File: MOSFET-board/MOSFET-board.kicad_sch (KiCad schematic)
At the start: 74 parts, among them J1 PCIE-LP-01-01-F-DV-A-TR, J2 DB25_Female, U1 BTS3080EJXUMA1, U10 BTS3080EJXUMA1, U11 PCF8575_Breakout, U2 BTS3080EJXUMA1, U3 BTS3080EJXUMA1, U4 BTS3080EJXUMA1, U5 BTS3080EJXUMA1, U6 BTS3080EJXUMA1, U7 BTS3080EJXUMA1, U8 BTS3080EJXUMA1, U9 BTS3080EJXUMA1

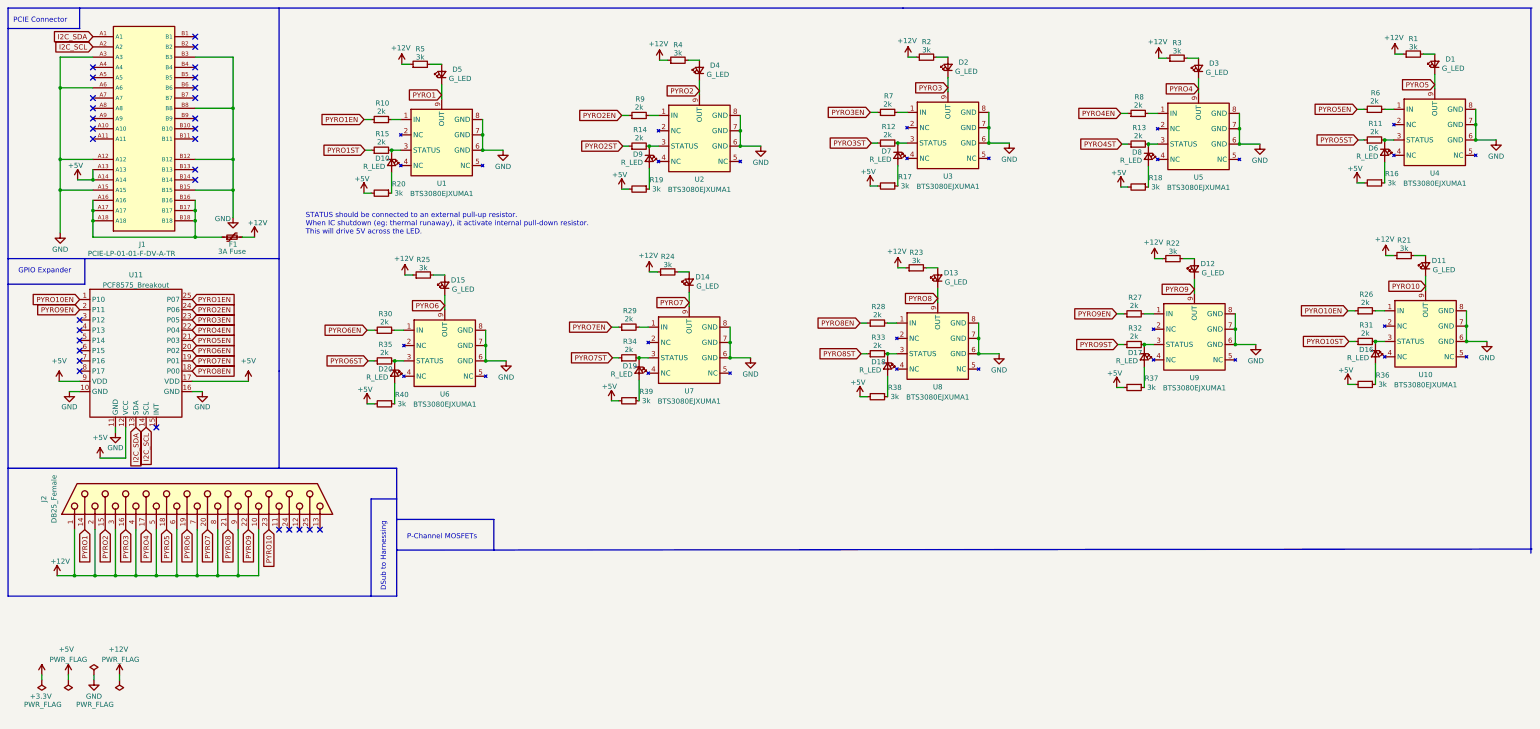
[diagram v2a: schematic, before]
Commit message: Updated HX, TC, and MOSFET board.
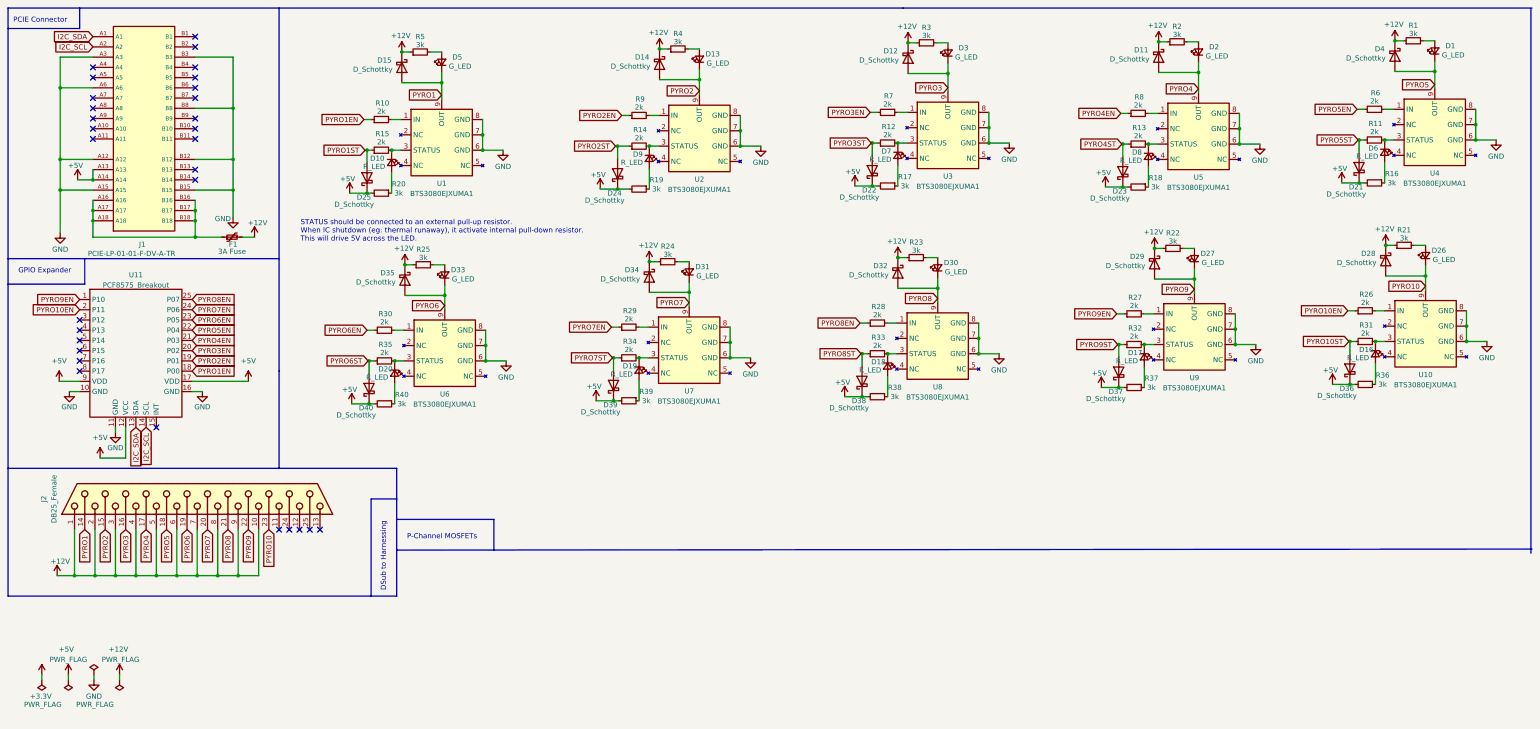
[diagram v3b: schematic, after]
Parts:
- removed D11, D12, D14, D15, D4: G_LED, LED_THT:LED_D1.8mm_W3.3mm_H2.4mm, symbol Device:LED_Small
- added D11, D12, D14, D15, D21, D22, D23, D24, D25, D28, D29, D32, D34, D35, D36, D37, D38, D39, D4, D40: D_Schottky, Diode_SMD:D_0603_1608Metric, symbol Device:D_Schottky
- added D26, D27, D30, D31, D33: G_LED, LED_THT:LED_D1.8mm_W3.3mm_H2.4mm, symbol Device:LED_Small
- F1: footprint (none) -> Fuse:Fuse_0603_1608Metric
- J1: footprint PCIe_x1_card_edge:PCIe_x1_card_edge -> Connector_PCBEdge:BUS_PCIexpress_x1
- R1, R10, R11, R12, R13, R14, R15, R16, R17, R18, R19, R2, R20, R21, R22, R23, R24, R25, R26, R27, R28, R29, R3, R30, R31, R32, R33, R34, R35, R36, R37, R38, R39, R4, R40, R5, R6, R7, R8, R9: footprint Resistor_SMD:R_0805_2012Metric -> Resistor_SMD:R_0603_1608Metric
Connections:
- net +12V: now also D11.1 (K), D12.1 (K), D14.1 (K), D15.1 (K), D28.1 (K), D29.1 (K), D32.1 (K), D34.1 (K), D35.1 (K), D4.1 (K)
- net +5V: now also D21.1 (K), D22.1 (K), D23.1 (K), D24.1 (K), D25.1 (K), D36.1 (K), D37.1 (K), D38.1 (K), D39.1 (K), D40.1 (K)
- net PYRO1: now also D15.2 (A)
- net PYRO10: now also D26.1 (K), D28.2 (A)
- net PYRO10EN: now also U11.2 (P11); no longer U11.1 (P10)
- net PYRO10ST: now also D36.2 (A)
- net PYRO1EN: now also U11.18 (P00); no longer U11.25 (P07)
- net PYRO1ST: now also D25.2 (A)
- net PYRO2: now also D13.1 (K), D14.2 (A)
- net PYRO2EN: now also U11.19 (P01); no longer U11.24 (P06)
- net PYRO2ST: now also D24.2 (A)
- net PYRO3: now also D3.1 (K), D12.2 (A); no longer D2.1 (K)
- net PYRO3EN: now also U11.20 (P02); no longer U11.23 (P05)
- net PYRO3ST: now also D22.2 (A)
- net PYRO4: now also D2.1 (K), D11.2 (A); no longer D3.1 (K)
- net PYRO4EN: now also U11.21 (P03); no longer U11.22 (P04)
- net PYRO4ST: now also D23.2 (A)
- net PYRO5: now also D4.2 (A)
- net PYRO5EN: now also U11.22 (P04); no longer U11.21 (P03)
- net PYRO5ST: now also D21.2 (A)
- net PYRO6: now also D33.1 (K), D35.2 (A)
- net PYRO6EN: now also U11.23 (P05); no longer U11.20 (P02)
- net PYRO6ST: now also D40.2 (A)
- net PYRO7: now also D31.1 (K), D34.2 (A)
- net PYRO7EN: now also U11.24 (P06); no longer U11.19 (P01)
- net PYRO7ST: now also D39.2 (A)
- net PYRO8: now also D30.1 (K), D32.2 (A); no longer D13.1 (K)
- net PYRO8EN: now also U11.25 (P07); no longer U11.18 (P00)
- net PYRO8ST: now also D38.2 (A)
- net PYRO9: now also D27.1 (K), D29.2 (A)
- net PYRO9EN: now also U11.1 (P10); no longer U11.2 (P11)
- net PYRO9ST: now also D37.2 (A)
- net at D13.2 (A): now also R4.2; no longer R23.2
- net at R25.2: now also D33.2 (A)
- net at R22.2: now also D27.2 (A)
- net at R24.2: now also D31.2 (A)
- net at R21.2: now also D26.2 (A)
- new net: D30.2 (A), R23.2
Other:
- moved on the sheet: D5, R5

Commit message: Updated pcie and fixed HX, MOSFET, TC board. Also added hierarchical sheet.
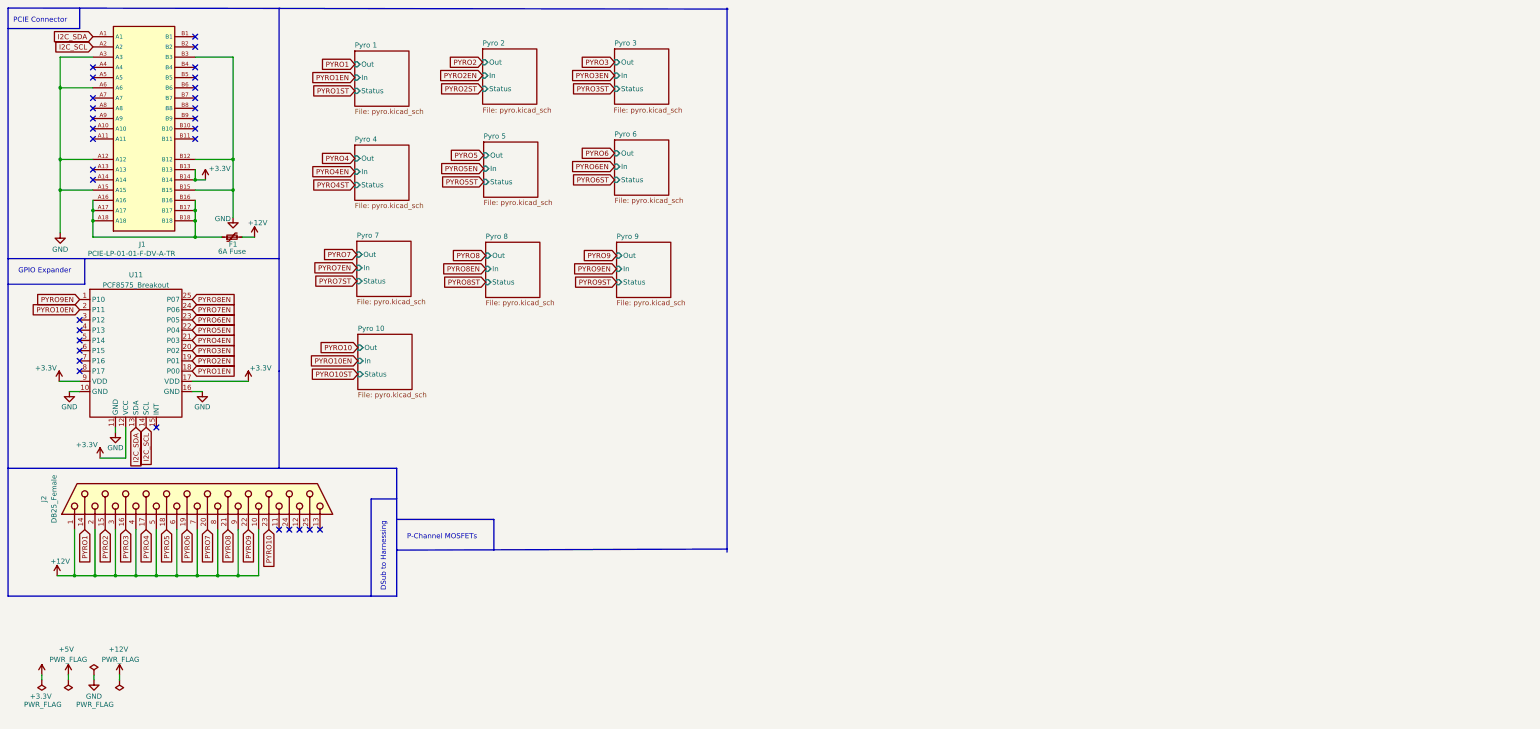
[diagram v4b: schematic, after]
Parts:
- removed D1, D13, D2, D26, D27, D3, D30, D31, D33, D5: G_LED, LED_THT:LED_D1.8mm_W3.3mm_H2.4mm, symbol Device:LED_Small
- removed D10, D16, D17, D18, D19, D20, D6, D7, D8, D9: R_LED, LED_THT:LED_D1.8mm_W3.3mm_H2.4mm, symbol Device:LED_Small
- removed D11, D12, D14, D15, D21, D22, D23, D24, D25, D28, D29, D32, D34, D35, D36, D37, D38, D39, D4, D40: D_Schottky, Diode_SMD:D_0603_1608Metric, symbol Device:D_Schottky
- removed R1, R16, R17, R18, R19, R2, R20, R21, R22, R23, R24, R25, R3, R36, R37, R38, R39, R4, R40, R5: 3k, Resistor_SMD:R_0603_1608Metric, symbol Device:R_Small
- removed R10, R11, R12, R13, R14, R15, R26, R27, R28, R29, R30, R31, R32, R33, R34, R35, R6, R7, R8, R9: 2k, Resistor_SMD:R_0603_1608Metric, symbol Device:R_Small
- removed U1, U10, U2, U3, U4, U5, U6, U7, U8, U9: BTS3080EJXUMA1, BTS3080EJXUMA1:SOIC127P600X115-9N, symbol BTS3080EJXUMA1:BTS3080EJXUMA1
- F1: value 3A Fuse -> 6A Fuse
- U11: footprint PCF875BreakoutBoard5:PCF8575_Breakout -> PCF8575_Breakout:PCF8575_Breakout
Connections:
- net +3.3V: now also J1.B13, J1.B14, U11.12 (VCC), U11.17 (VDD), U11.9 (VDD)
- net +5V: no longer J1.A13, J1.A14, U11.12 (VCC), U11.17 (VDD), U11.9 (VDD)
- net GND: no longer J1.B8
- no-connect marks 30 -> 31
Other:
- added sheet Pyro 1 (pyro.kicad_sch)
- added sheet Pyro 10 (pyro.kicad_sch)
- added sheet Pyro 2 (pyro.kicad_sch)
- added sheet Pyro 3 (pyro.kicad_sch)
- added sheet Pyro 4 (pyro.kicad_sch)
- added sheet Pyro 5 (pyro.kicad_sch)
- added sheet Pyro 6 (pyro.kicad_sch)
- added sheet Pyro 7 (pyro.kicad_sch)
- added sheet Pyro 8 (pyro.kicad_sch)
- added sheet Pyro 9 (pyro.kicad_sch)
- note removed: "STATUS should be connected to an external pull-up resistor. When IC shutdown (eg: thermal runaway), it activate internal pull-down resistor. This will drive 5V across the LED."

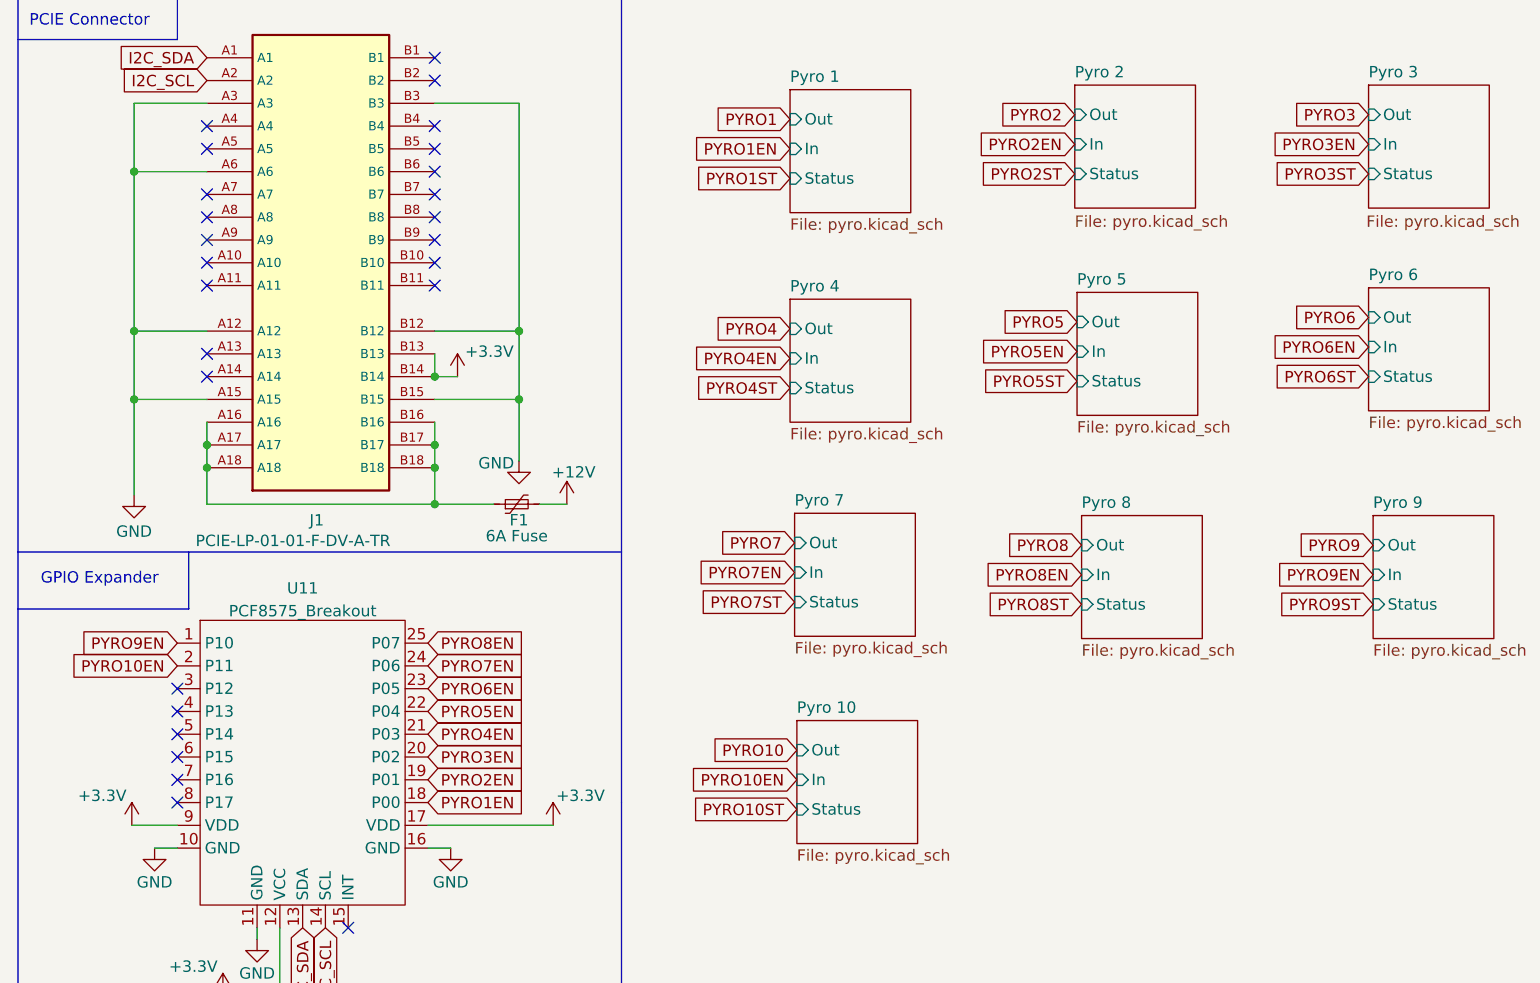
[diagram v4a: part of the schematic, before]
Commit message: Basic routing for MOSFET board. Need silkscreen update.
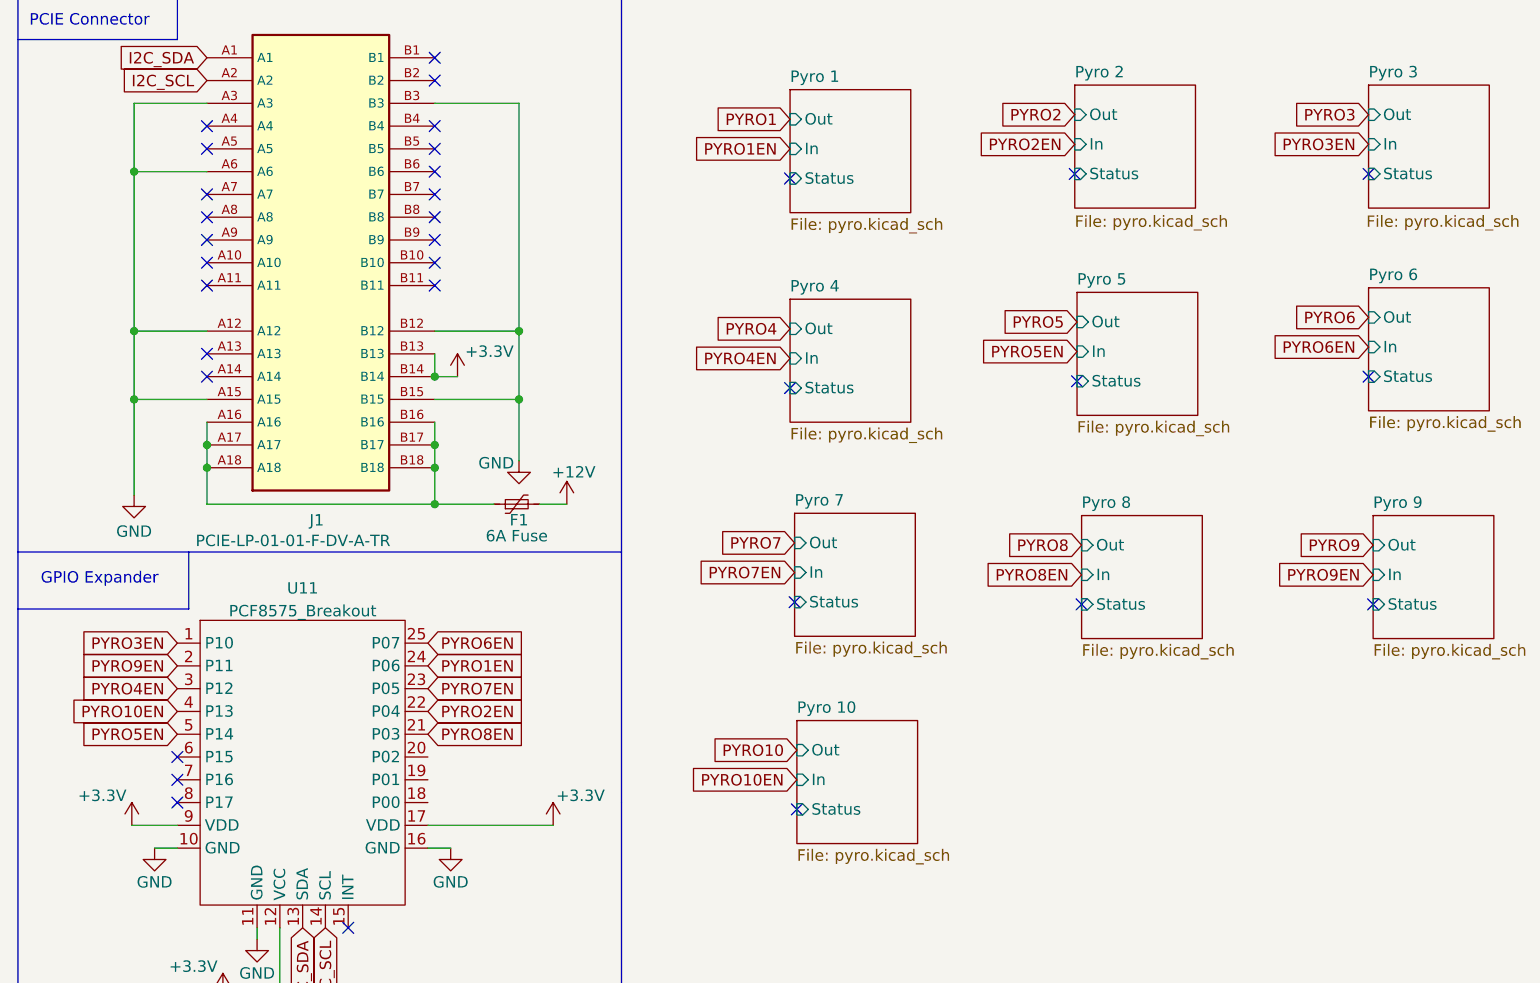
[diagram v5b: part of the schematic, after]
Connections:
- net PYRO10EN: now also U11.4 (P13); no longer U11.2 (P11)
- net PYRO1EN: now also U11.24 (P06); no longer U11.18 (P00)
- net PYRO2EN: now also U11.22 (P04); no longer U11.19 (P01)
- net PYRO3EN: now also U11.1 (P10); no longer U11.20 (P02)
- net PYRO4EN: now also U11.3 (P12); no longer U11.21 (P03)
- net PYRO5EN: now also U11.5 (P14); no longer U11.22 (P04)
- net PYRO6EN: now also U11.25 (P07); no longer U11.23 (P05)
- net PYRO7EN: now also U11.23 (P05); no longer U11.24 (P06)
- net PYRO8EN: now also U11.21 (P03); no longer U11.25 (P07)
- net PYRO9EN: now also U11.2 (P11); no longer U11.1 (P10)
- no-connect marks 31 -> 38
